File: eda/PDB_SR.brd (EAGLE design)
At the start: 101.6 x 81.3 mm, 18 parts

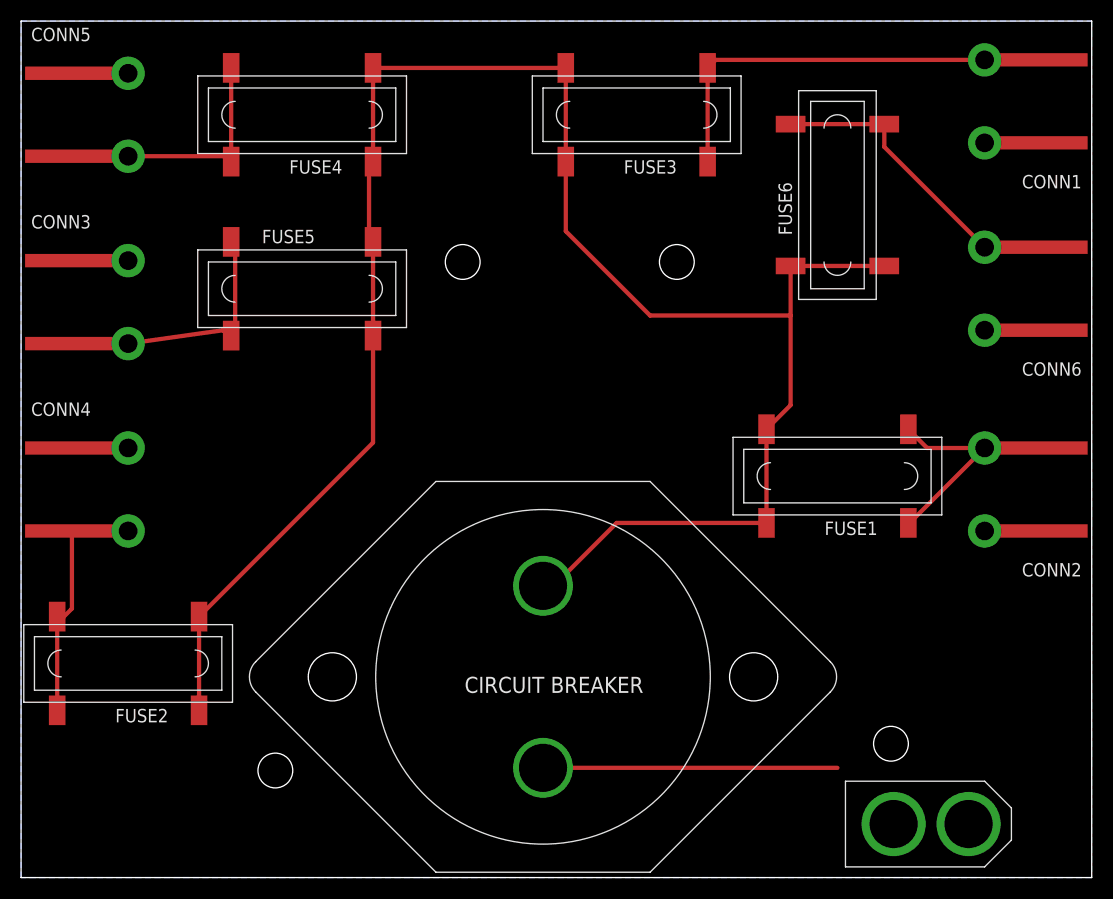
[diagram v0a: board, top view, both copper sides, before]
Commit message: Renamed wires from Fuses (N,N, etc) to VOUT_
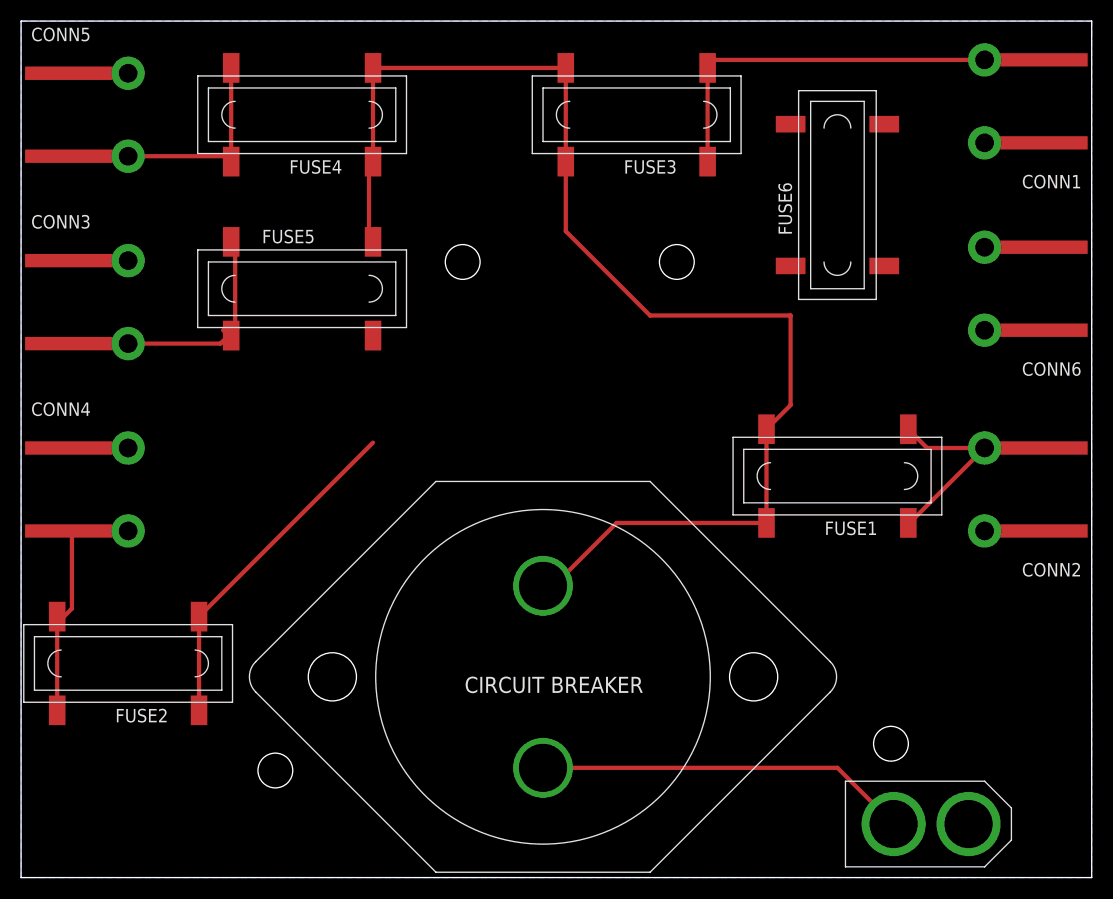
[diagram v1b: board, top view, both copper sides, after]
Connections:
- net N$1 renamed VOUT1
- net N$2 renamed VOUT4
- net N$3 renamed VOUT3
- net N$4 renamed VOUT5
- net N$5 renamed VOUT2
- net N$7 renamed VOUT6
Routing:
- net 12V: track 190.2 -> 156.3 mm
- net VOUT6: track 29.9 -> 0.00 mm
- net BAT: track 27.9 -> 35.5 mm
- net VOUT5: track 26.0 -> 27.6 mm
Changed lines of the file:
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@@
 <wire x1="97.79" y1="52.07" x2="96.901" y2="52.07" width="0.4064" layer="1"/>
 <wire x1="96.901" y1="52.07" x2="96.774" y2="51.943" width="0.4064" layer="1"/>
-<wire x1="96.901" y1="52.07" x2="96.774" y2="69.723" width="0" layer="19" extent="1-1"/>
-<wire x1="96.774" y1="32.893" x2="97.663" y2="51.943" width="0" layer="19" extent="1-1"/>
-<wire x1="89.916" y1="5.08" x2="91.44" y2="32.893" width="0" layer="19" extent="1-1"/>
-<wire x1="10.16" y1="76.327" x2="91.44" y2="69.723" width="0" layer="19" extent="1-1"/>
-<wire x1="10.16" y1="58.547" x2="10.16" y2="76.327" width="0" layer="19" extent="1-1"/>
-<wire x1="10.16" y1="40.767" x2="10.16" y2="58.547" width="0" layer="19" extent="1-1"/>
 </signal>
 <signal name="12V">
@@
 <contactref element="FUSE4" pad="P$1_UP"/>
 <contactref element="FUSE4" pad="P$1_DOWN"/>
-<contactref element="FUSE5" pad="P$2_UP"/>
-<contactref element="FUSE5" pad="P$2_DOWN"/>
-<contactref element="FUSE6" pad="P$1_UP"/>
-<contactref element="FUSE6" pad="P$1_DOWN"/>
 <contactref element="CIRCUIT_BREAKER" pad="P$2"/>
 <wire x1="51.435" y1="76.835" x2="52.07" y2="76.2" width="0.4064" layer="1"/>
 <wire x1="52.07" y1="76.2" x2="52.07" y2="76.454" width="0.4064" layer="1"/>
 <wire x1="52.07" y1="76.454" x2="51.689" y2="76.835" width="0.4064" layer="1"/>
-<wire x1="81.915" y1="58.039" x2="73.025" y2="58.039" width="0.4064" layer="1"/>
-<wire x1="73.025" y1="58.039" x2="73.025" y2="53.34" width="0.4064" layer="1"/>
 <wire x1="73.025" y1="53.34" x2="73.025" y2="44.831" width="0.4064" layer="1"/>
 <wire x1="73.025" y1="44.831" x2="70.739" y2="42.545" width="0.4064" layer="1"/>
@@
 <wire x1="33.02" y1="67.31" x2="33.02" y2="59.944" width="0.4064" layer="1"/>
 <wire x1="33.02" y1="59.69" x2="33.02" y2="59.944" width="0.4064" layer="1"/>
-<wire x1="33.02" y1="59.944" x2="33.401" y2="60.325" width="0.4064" layer="1"/>
-<wire x1="33.401" y1="60.325" x2="33.401" y2="51.435" width="0.4064" layer="1"/>
-<wire x1="33.401" y1="51.435" x2="33.401" y2="51.181" width="0.4064" layer="1"/>
-<wire x1="33.401" y1="51.181" x2="33.02" y2="50.8" width="0.4064" layer="1"/>
-<wire x1="33.401" y1="51.435" x2="33.401" y2="41.275" width="0.4064" layer="1"/>
 <wire x1="33.401" y1="41.275" x2="16.891" y2="24.765" width="0.4064" layer="1"/>
 <wire x1="16.891" y1="24.765" x2="16.891" y2="15.875" width="0.4064" layer="1"/>
@@
 <wire x1="51.689" y1="61.341" x2="59.69" y2="53.34" width="0.4064" layer="1"/>
 <wire x1="59.69" y1="53.34" x2="73.025" y2="53.34" width="0.4064" layer="1"/>
+<contactref element="FUSE5" pad="P$2_UP"/>
+<contactref element="FUSE5" pad="P$2_DOWN"/>
+<contactref element="FUSE6" pad="P$1_UP"/>
+<contactref element="FUSE6" pad="P$1_DOWN"/>
+<wire x1="73.025" y1="58.039" x2="81.915" y2="58.039" width="0" layer="19" extent="1-1"/>
+<wire x1="73.025" y1="53.34" x2="73.025" y2="58.039" width="0" layer="19" extent="1-1"/>
+<wire x1="33.401" y1="60.325" x2="33.02" y2="59.944" width="0" layer="19" extent="1-1"/>
+<wire x1="33.401" y1="51.435" x2="33.02" y2="59.69" width="0" layer="19" extent="1-1"/>
+<wire x1="33.401" y1="41.275" x2="33.401" y2="51.435" width="0" layer="19" extent="1-1"/>
 </signal>
-<signal name="N$1">
+<signal name="VOUT1">
 <contactref element="CONN2" pad="PIN2"/>
 <contactref element="CONN2" pad="PIN2-LEAD"/>
@@
 <wire x1="96.647" y1="40.64" x2="96.774" y2="40.767" width="0.4064" layer="1"/>
 </signal>
-<signal name="N$3">
+<signal name="VOUT3">
 <contactref element="CONN1" pad="PIN2"/>
 <contactref element="CONN1" pad="PIN2-LEAD"/>
@@
 <wire x1="91.44" y1="77.597" x2="96.774" y2="77.597" width="0.4064" layer="1"/>
 </signal>
-<signal name="N$5">
+<signal name="VOUT2">
 <contactref element="CONN4" pad="PIN2"/>
 <contactref element="CONN4" pad="PIN2-LEAD"/>
@@
 <wire x1="4.826" y1="25.527" x2="3.429" y2="24.13" width="0.4064" layer="1"/>
 </signal>
-<signal name="N$2">
+<signal name="VOUT4">
 <contactref element="FUSE4" pad="P$2_UP"/>
 <contactref element="FUSE4" pad="P$2_DOWN"/>
@@
 <wire x1="10.16" y1="68.453" x2="4.826" y2="68.453" width="0.4064" layer="1"/>
 </signal>
-<signal name="N$4">
+<signal name="VOUT5">
 <contactref element="FUSE5" pad="P$1_UP"/>
 <contactref element="FUSE5" pad="P$1_DOWN"/>
 <contactref element="CONN3" pad="PIN2"/>
 <contactref element="CONN3" pad="PIN2-LEAD"/>
-<wire x1="4.826" y1="50.673" x2="10.16" y2="50.673" width="0.4064" layer="1"/>
-<wire x1="20.32" y1="50.8" x2="20.32" y2="59.944" width="0.4064" layer="1"/>
+<wire x1="20.32" y1="50.8" x2="20.32" y2="52.07" width="0.4064" layer="1"/>
+<wire x1="20.32" y1="52.07" x2="20.32" y2="59.944" width="0.4064" layer="1"/>
 <wire x1="20.32" y1="59.944" x2="19.939" y2="60.325" width="0.4064" layer="1"/>
-<wire x1="10.16" y1="50.673" x2="19.177" y2="51.943" width="0.4064" layer="1"/>
 <wire x1="19.177" y1="51.943" x2="19.939" y2="51.181" width="0.4064" layer="1"/>
 <wire x1="19.939" y1="51.435" x2="19.939" y2="51.181" width="0.4064" layer="1"/>
 <wire x1="19.939" y1="51.181" x2="20.32" y2="50.8" width="0.4064" layer="1"/>
-</signal>
-<signal name="N$7">
-<contactref element="FUSE6" pad="P$2_UP"/>
-<contactref element="FUSE6" pad="P$2_DOWN"/>
-<contactref element="CONN6" pad="PIN2"/>
-<contactref element="CONN6" pad="PIN2-LEAD"/>
-<wire x1="73.025" y1="71.501" x2="81.915" y2="71.501" width="0.4064" layer="1"/>
-<wire x1="81.915" y1="71.501" x2="81.915" y2="69.342" width="0.4064" layer="1"/>
-<wire x1="81.915" y1="69.342" x2="91.44" y2="59.817" width="0.4064" layer="1"/>
-<wire x1="91.44" y1="59.817" x2="96.774" y2="59.817" width="0.4064" layer="1"/>
+<wire x1="10.16" y1="50.673" x2="4.826" y2="50.673" width="0.4064" layer="1"/>
+<wire x1="10.16" y1="50.673" x2="18.923" y2="50.673" width="0.4064" layer="1"/>
+<wire x1="18.923" y1="50.673" x2="20.32" y2="52.07" width="0.4064" layer="1"/>
 </signal>
 <signal name="BAT">
@@
 <wire x1="49.53" y1="10.414" x2="77.47" y2="10.414" width="0.4064" layer="1"/>
 <contactref element="U$1" pad="12V"/>
-<wire x1="77.47" y1="10.414" x2="82.804" y2="5.08" width="0" layer="19" extent="1-1"/>
+<wire x1="77.47" y1="10.414" x2="82.804" y2="5.08" width="0.4064" layer="1"/>
+</signal>
+<signal name="VOUT6">
+<contactref element="FUSE6" pad="P$2_UP"/>
+<contactref element="FUSE6" pad="P$2_DOWN"/>
+<contactref element="CONN6" pad="PIN2"/>
+<contactref element="CONN6" pad="PIN2-LEAD"/>
+<wire x1="91.44" y1="59.817" x2="96.774" y2="59.817" width="0" layer="19" extent="1-1"/>
+<wire x1="81.915" y1="71.501" x2="91.44" y2="59.817" width="0" layer="19" extent="1-1"/>
+<wire x1="73.025" y1="71.501" x2="81.915" y2="71.501" width="0" layer="19" extent="1-1"/>
 </signal>
 </signals>

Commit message: Moved Holes toward outer edges
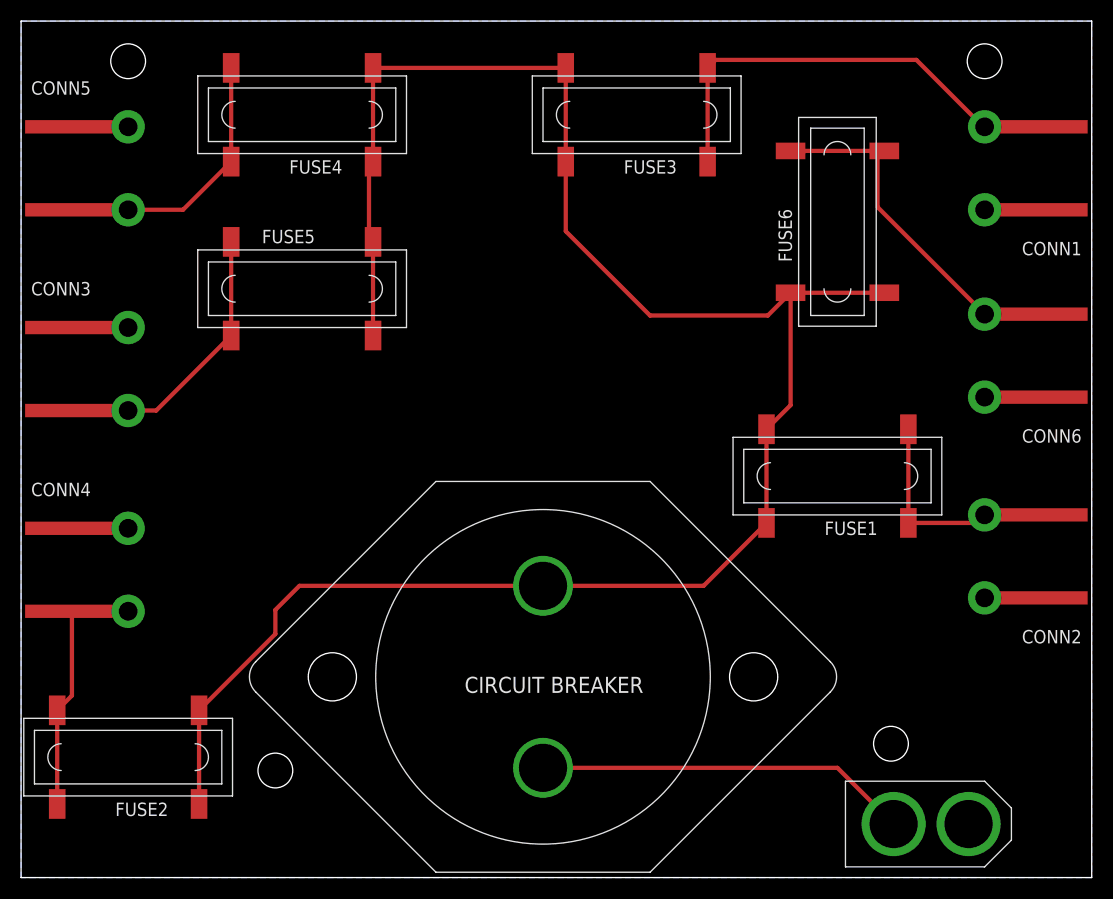
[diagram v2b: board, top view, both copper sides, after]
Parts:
- moved U$3 37.0 mm to (10.2, 77.5)
- moved U$4 34.9 mm to (91.4, 77.5)
- moved FUSE2 8.89 mm to (10.2, 11.4)
- moved CONN4 7.62 mm to (10.2, 29.2)
- moved CONN3 6.35 mm to (10.2, 48.3)
- moved CONN6 6.35 mm to (91.4, 49.5)
- moved CONN2 6.35 mm to (91.4, 30.5)
- moved CONN1 6.35 mm to (91.4, 67.3)
- moved CONN5 5.08 mm to (10.2, 67.3)
- moved FUSE6 2.54 mm to (77.5, 62.2)
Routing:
- net VOUT6: track 0.00 -> 34.3 mm
- net 12V: track 156.3 -> 189.9 mm
- net VOUT1: track 31.1 -> 21.8 mm
- net VOUT3: track 40.8 -> 43.6 mm
- net VOUT4: track 26.3 -> 28.7 mm
- net GND: track 34.1 -> 32.0 mm
- net VOUT5: track 27.6 -> 26.9 mm
- net VOUT2: track 23.6 -> 24.2 mm
